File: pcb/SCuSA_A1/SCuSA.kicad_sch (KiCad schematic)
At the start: 51 parts, among them J101 USB4135-GF-A, J102 JST_S2B-PH-K-x, J103 Binding_Post_PK4_Red, J104 Binding_Post_PK4_Black, J105 Binding_Post_PK4_Red, J106 Binding_Post_PK4_Black, Q101 DMN2041LSD, SW101 JS202011CQN, SW102 JS202011CQN, U101 MCP73832T-2ACI/OT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

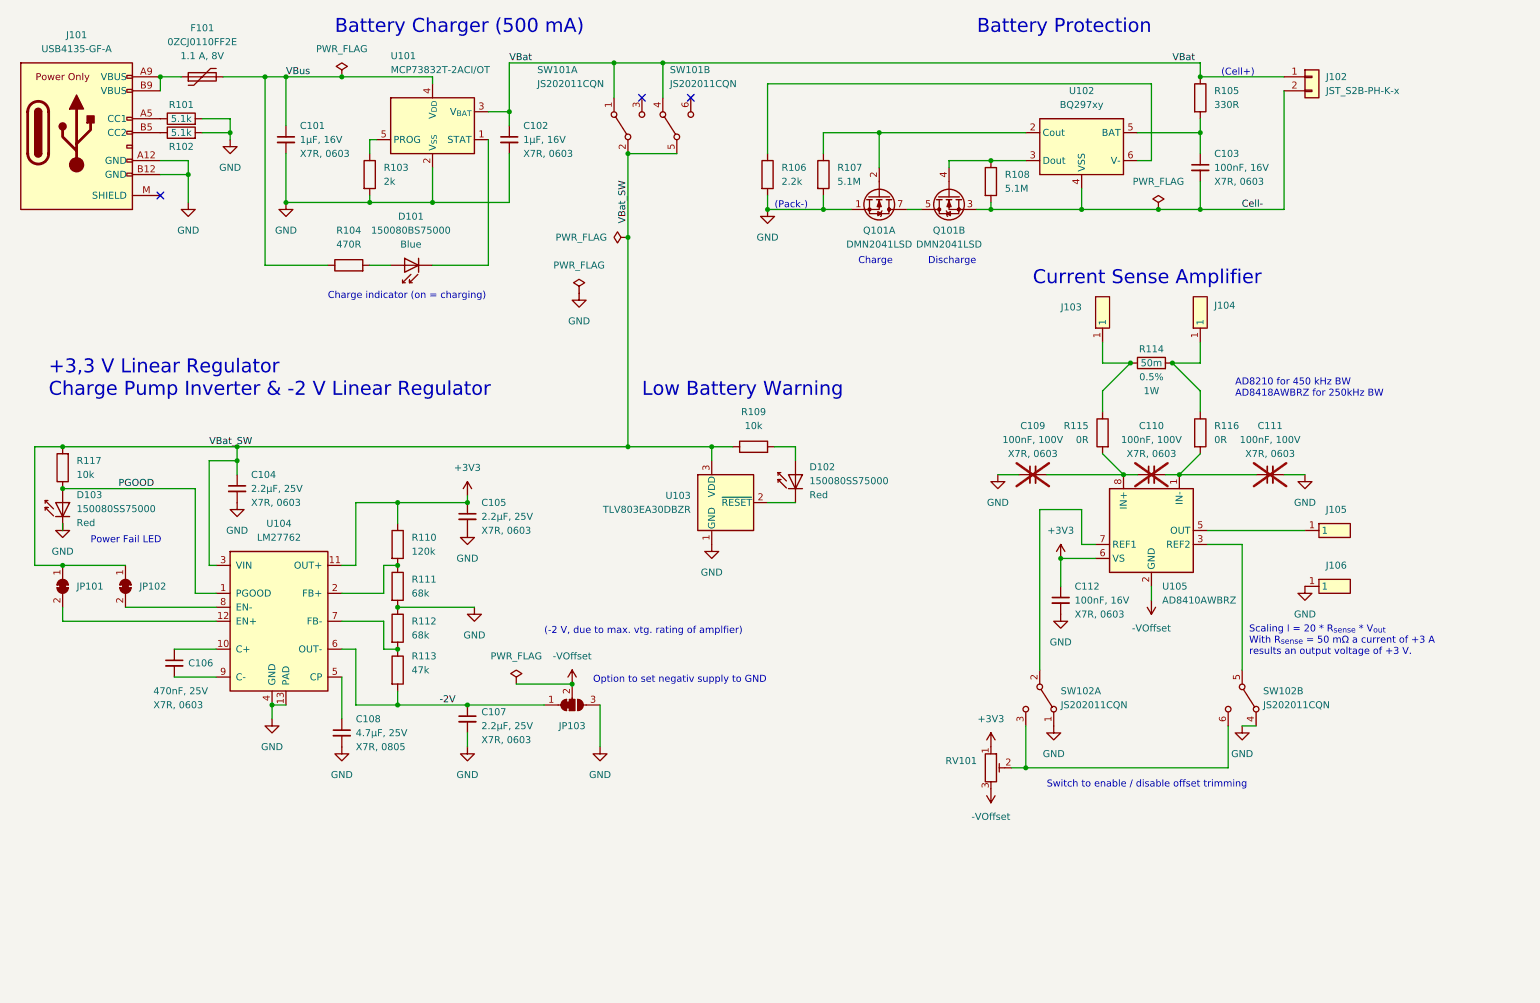
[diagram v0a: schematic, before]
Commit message: Add connectors, supply voltage filter
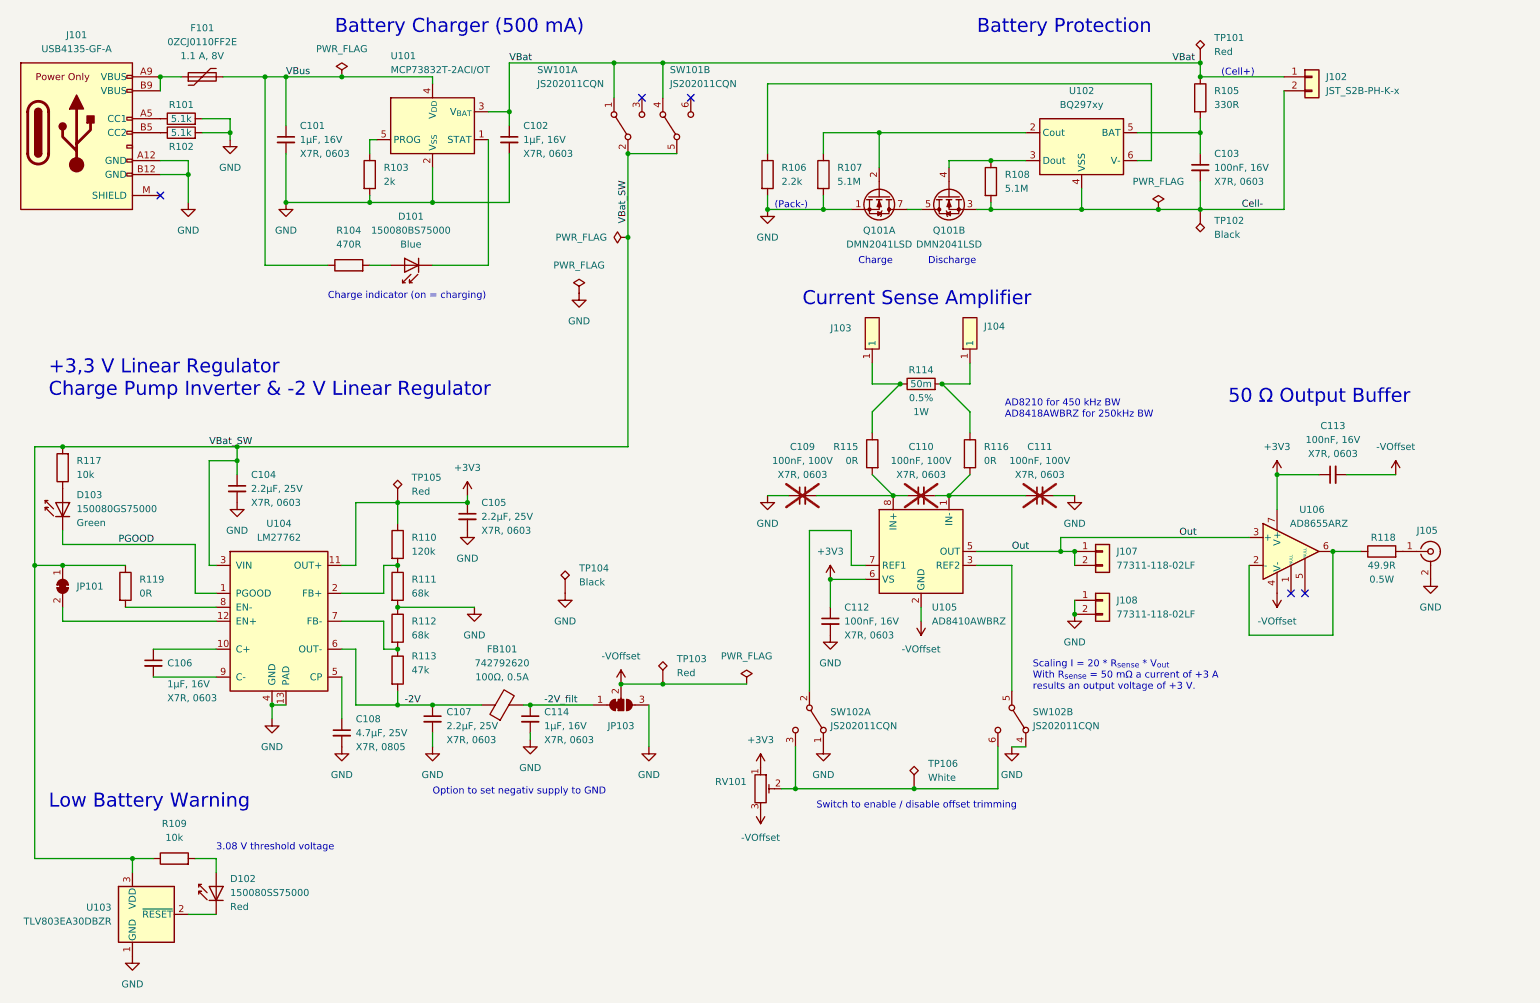
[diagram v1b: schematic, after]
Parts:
- removed D103: 150080SS75000, LED_SMD:LED_0805_2012Metric_Pad1.15x1.40mm_HandSolder, symbol LED_User:150080SS75000
- removed J105: Binding_Post_PK4_Red, Connector_User:Binding_Post_4.3mm_M4_DIN965_Pad, symbol Connector_User:Binding_Post_PK4_Red
- removed J106: Binding_Post_PK4_Black, Connector_User:Binding_Post_4.3mm_M4_DIN965_Pad, symbol Connector_User:Binding_Post_PK4_Black
- removed JP102: SolderJumper_2_Bridged, Jumper:SolderJumper-2_P1.3mm_Bridged_Pad1.0x1.5mm, symbol Jumper:SolderJumper_2_Bridged
- added C113: 100nF,16V,X7R,0603, Capacitor_SMD:C_0603_1608Metric_Pad1.08x0.95mm_HandSolder, symbol Capacitor_User:100nF,16V,X7R,0603
- added C114: 1uF,16V,X7R,0603, Capacitor_SMD:C_0603_1608Metric_Pad1.08x0.95mm_HandSolder, symbol Capacitor_User:1uF,16V,X7R,0603
- added D103: 150080GS75000, LED_SMD:LED_0805_2012Metric_Pad1.15x1.40mm_HandSolder, symbol LED_User:150080GS75000
- added FB101: 742792620, Inductor_SMD:L_1206_3216Metric_Pad1.42x1.75mm_HandSolder, symbol Ferrite_User:742792620
- added J105: SMA_Straight_Jack_Female, Connector_Coaxial:SMA_Wurth_60312002114503_Vertical, symbol Connector_User:SMA_Straight_Jack_Female
- added J107, J108: 77311-118-02LF, Connector_PinHeader_2.54mm:PinHeader_1x02_P2.54mm_Vertical, symbol Connector_User:77311-118-02LF
- added R118: 49.9R,1206, Resistor_SMD:R_1206_3216Metric_Pad1.30x1.75mm_HandSolder, symbol Resistor_User:49.9R,1206
- added R119: 0R,0603, Resistor_SMD:R_0603_1608Metric_Pad0.98x0.95mm_HandSolder, symbol Resistor_User:0R,0603
- added TP101, TP103, TP105: TestPoint_5010_Red, TestPoint:TestPoint_Loop_D2.60mm_Drill1.6mm_Beaded, symbol Testpoint_User:TestPoint_5010_Red
- added TP102, TP104: TestPoint_5011_Black, TestPoint:TestPoint_Loop_D2.60mm_Drill1.6mm_Beaded, symbol Testpoint_User:TestPoint_5011_Black
- added TP106: TestPoint_5012_White, TestPoint:TestPoint_Loop_D2.60mm_Drill1.6mm_Beaded, symbol Testpoint_User:TestPoint_5012_White
- added U106: AD8655ARZ, Package_SO:SOIC-8_3.9x4.9mm_P1.27mm, symbol Amplifier_Operational:AD8655
- C106: symbol Capacitor_User:470nF,25V,X7R,0603 -> Capacitor_User:1uF,16V,X7R,0603; Pretty Value 1 470nF, 25V -> 1μF, 16V
- R114: footprint Resistor_SMD:R_1206_3216Metric -> Resistor_SMD:R_1206_3216Metric_Pad1.30x1.75mm_HandSolder
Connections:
- net +3V3: now also C113.1, TP105.1, U106.7 (V+)
- net -2V: now also FB101.1; no longer JP103.1 (A)
- net -VOffset: now also C113.2, TP103.1, U106.4 (V-)
- net Cell-: now also TP102.1
- net GND: now also C114.2, J105.2 (Ext), J108.1 (Pin_1), J108.2 (Pin_2), TP104.1
- net PGOOD: now also D103.1 (K); no longer R117.1
- net VBat: now also TP101.1
- net VBat_SW: now also R119.1
- net Out: now reaches U105.5 (OUT)
- net Out: now also J107.1 (Pin_1), J107.2 (Pin_2), U106.3 (+)
- net at RV101.2, SW102.3 (C), SW102.6 (C): now also TP106.1
- net at U104.8 (EN-): now also R119.2
- new net: D103.2 (A), R117.1
- new net: R118.1, U106.2 (-), U106.6
- new net: J105.1 (In), R118.2
- new net -2V_filt: C114.1, FB101.2, JP103.1 (A)
- no-connect marks 3 -> 5
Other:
- note added: "3.08 V threshold voltage"
- note added: "50 Ω Output Buffer"
- note removed: "(-2 V, due to max. vtg. rating of amplfier)"
- note removed: "Power Fail LED"
- moved on the sheet: C106, C107, C109, C110, C111, C112, J103, J104, JP103, R114, R115, R116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

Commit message: Preliminary BOM
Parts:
- C106: value 470nF,25V,X7R,0603 -> 1uF,16V,X7R,0603
- R113: value 120k,0603 -> 47k,0603
- U102: value BQ297xy -> BQ29700DSER
- U104: SPN (none) -> 296-47331-1-ND; Supplier (none) -> Digi-Key
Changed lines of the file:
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@@
       (effects (font (size 1.27 1.27)))
     )
-    (property "Value" "BQ297xy" (at 214.63 33.02 0)
+    (property "Value" "BQ29700DSER" (at 214.63 33.02 0)
       (effects (font (size 1.27 1.27)))
     )
@@
     )
     (property "Datasheet" "http://www.ti.com/lit/ds/symlink/lm27762.pdf" (at 130.81 132.08 0)
+      (effects (font (size 1.27 1.27)) hide)
+    )
+    (property "Supplier" "Digi-Key" (at 67.31 121.92 0)
+      (effects (font (size 1.27 1.27)) hide)
+    )
+    (property "SPN" "296-47331-1-ND" (at 67.31 121.92 0)
       (effects (font (size 1.27 1.27)) hide)
     )
@@
       (effects (font (size 1.27 1.27)) (justify left))
     )
-    (property "Value" "120k,0603" (at 92.075 133.35 0)
+    (property "Value" "47k,0603" (at 92.075 133.35 0)
       (effects (font (size 1.27 1.27)) (justify left) hide)
     )
@@
       (effects (font (size 1.27 1.27)) (justify left))
     )
-    (property "Value" "470nF,25V,X7R,0603" (at 48.26 139.7 0)
-      (effects (font (size 1.27 1.27)) (justify left) hide)
-    )
+    (property "Value" "1uF,16V,X7R,0603" (at 48.26 139.7 0)
+      (effects (font (size 1.27 1.27)) (justify left) hide)
+    )

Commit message: Work on PCB layout
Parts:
- added TP107: TestPoint_5011_Black, TestPoint:TestPoint_Loop_D2.60mm_Drill1.6mm_Beaded, symbol Testpoint_User:TestPoint_5011_Black
- added TP108: TestPoint_5010_Red, TestPoint:TestPoint_Loop_D2.60mm_Drill1.6mm_Beaded, symbol Testpoint_User:TestPoint_5010_Red
- J103: footprint Connector_User:Binding_Post_4.3mm_M4_DIN965_Pad -> Connector_User:Binding_Post_PK4_Red
- J104: footprint Connector_User:Binding_Post_4.3mm_M4_DIN965_Pad -> Connector_User:Binding_Post_PK4_Black
- J105: footprint Connector_Coaxial:SMA_Wurth_60312002114503_Vertical -> Connector_User:SMA_Vertical
- RV101: footprint Potentionmeter_THT_User:Potentiometer_Suntan_3296W_Vertical -> Potentionmeter_THT_User:Potentiometer_Suntan_3296W_Vertical_90deg
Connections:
- net -VOffset: now also C112.2
- net GND: now also TP107.1; no longer C112.2
- net Out: now also TP108.1
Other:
- moved on the sheet: SW102A

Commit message: Edit PCB layout
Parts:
- removed JP101: SolderJumper_2_Bridged, Jumper:SolderJumper-2_P1.3mm_Bridged_Pad1.0x1.5mm, symbol Jumper:SolderJumper_2_Bridged
- added H101, H102, H103, H104: MountingHole, MountingHole:MountingHole_3.2mm_M3_DIN965, symbol Mechanical:MountingHole
- added JP101: SolderJumper_2_Open, Jumper:SolderJumper-2_P1.3mm_Open_TrianglePad1.0x1.5mm, symbol Jumper:SolderJumper_2_Open
- added R120: 0R,0603, Resistor_SMD:R_0603_1608Metric_Pad0.98x0.95mm_HandSolder, symbol Resistor_User:0R,0603
- R103: value 2k,0603 -> 10k,0603; symbol Resistor_User:2k,0603 -> Resistor_User:10k,0603; Resistance 2k -> 10k
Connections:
- net Cell-: now also JP101.2 (B)
- net GND: now also JP101.1 (A)
- net VBat_SW: now also R120.1
- net at U104.12 (EN+): now also R120.2
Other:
- note added: "Charging current ~ 100 mA"
- note added: "For battery pack with integrated protection."

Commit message: Edit PCB layout
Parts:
- JP103: value SolderJumper_3_Bridged12 -> SolderJumper_3_Open; footprint Jumper:SolderJumper-3_P1.3mm_Bridged12_Pad1.0x1.5mm_NumberLabels -> Jumper:SolderJumper-3_P2.0mm_Open_TrianglePad1.0x1.5mm_NumberLabels; symbol Jumper:SolderJumper_3_Bridged12 -> Jumper:SolderJumper_3_Open
- U104: footprint Package_SON:WSON-12-1EP_3x2mm_P0.5mm_EP1x2.65_ThermalVias -> Package_SON_User:WSON-12-1EP_3x2mm_P0.5mm_EP1x2.65_ThermalVias; symbol Regulator_SwitchedCapacitor:LM27762 -> Regulator_Switching_User:LM27762; MPN (none) -> LM27762DSSx; Manufacturer (none) -> Texas Instruments
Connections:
- net GND: no longer C109.1, C111.2
- net SNS-2: now reaches C110.2, C111.1, R116.2, U105.1 (IN-)
- net SNS+2: now reaches C109.2, C110.1, R115.2, U105.8 (IN+)
- net SNS-1: now reaches J104.1, R114.2, R116.1
- net SNS+1: now reaches J103.1, R114.1, R115.1
- net -VOffset renamed -Vx
- net -Vx: now also C109.1, C111.2
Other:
- moved on the sheet: J103, J104

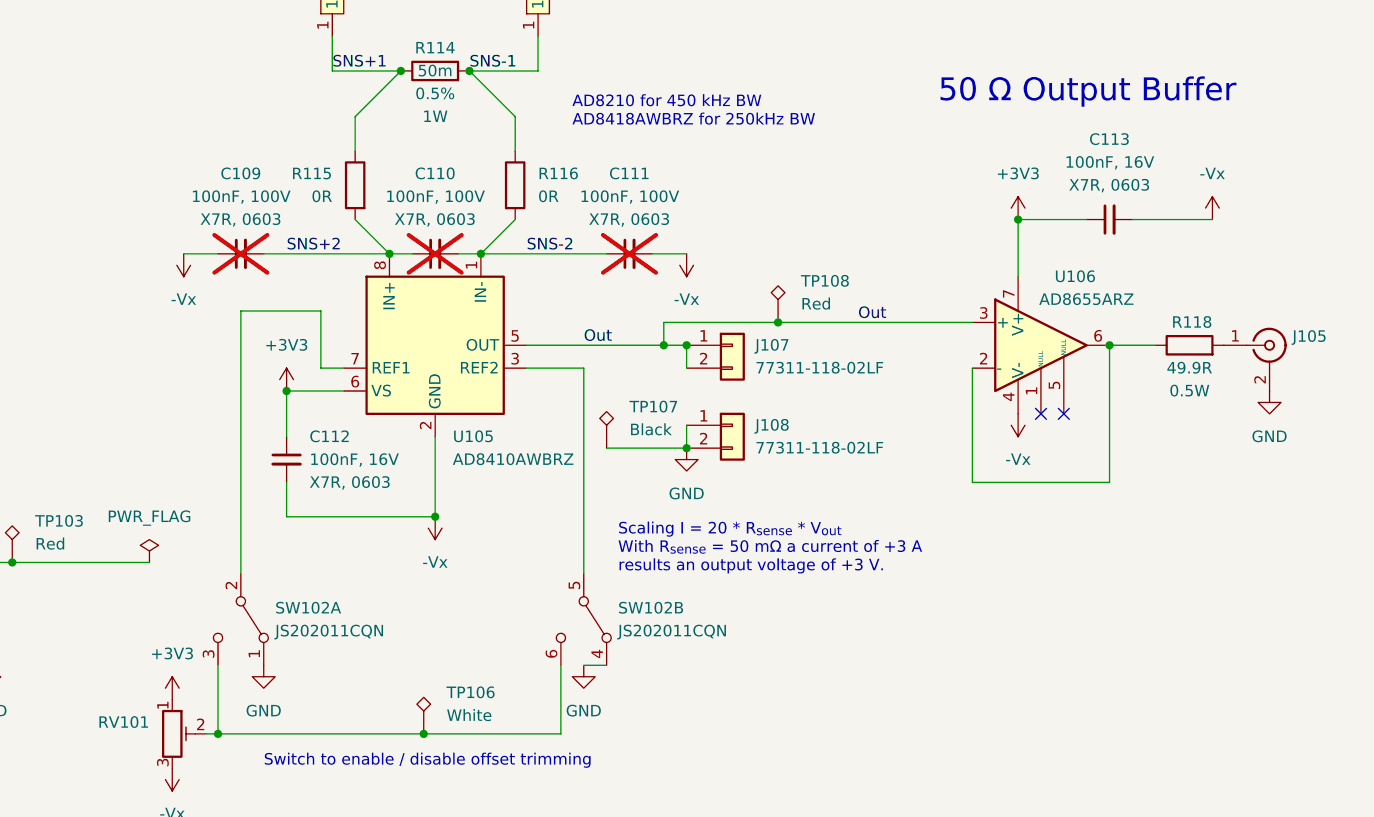
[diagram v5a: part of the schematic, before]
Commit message: Change binding posts and GND planes
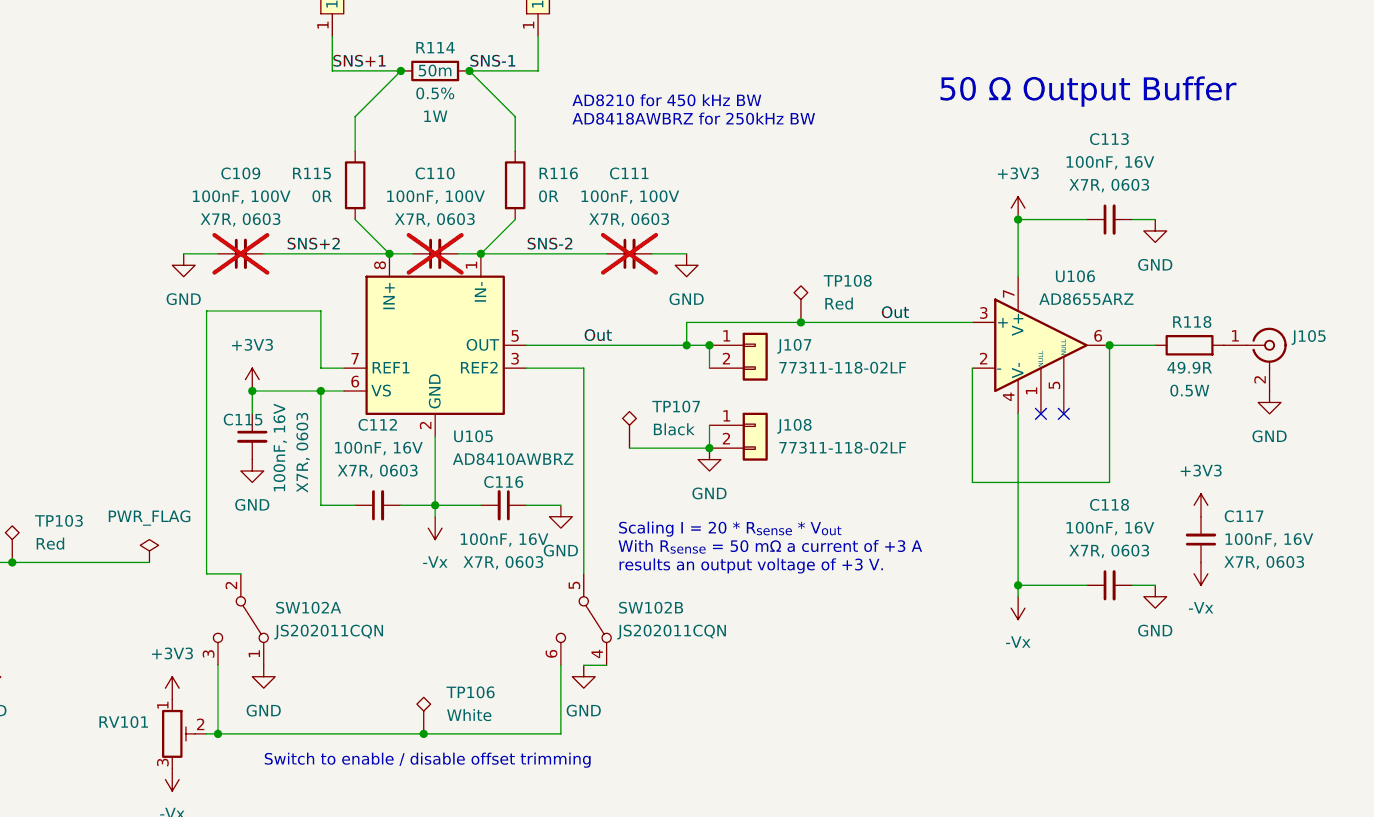
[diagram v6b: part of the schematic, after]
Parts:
- added C115, C116, C117, C118: 100nF,16V,X7R,0603, Capacitor_SMD:C_0603_1608Metric_Pad1.08x0.95mm_HandSolder, symbol Capacitor_User:100nF,16V,X7R,0603
- J103: value Binding_Post_PK4_Red -> Binding_Post_PKI_10_A_Au; footprint Connector_User:Binding_Post_PK4_Red -> Connector_User:Binding_Post_PKI_10_A_Au_Red; symbol Connector_User:Binding_Post_PK4_Red -> Connector_User:Binding_Post_PKI_10_A_Au_Red; MPN (none) -> 930103701; Manufacturer (none) -> SKS, Hirschmann; SPN PK 4 RT -> PKI 10 A AU RT
- J104: value Binding_Post_PK4_Black -> Binding_Post_PKI_10_A_Au; footprint Connector_User:Binding_Post_PK4_Black -> Connector_User:Binding_Post_PKI_10_A_Au_Black; symbol Connector_User:Binding_Post_PK4_Black -> Connector_User:Binding_Post_PKI_10_A_Au_Black; MPN (none) -> 930103700; Manufacturer (none) -> SKS, Hirschmann; SPN PK 4 SW -> PKI 10 A AU SW
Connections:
- net +3V3: now also C115.1, C117.2
- net -Vx: now also C116.2, C117.1, C118.1; no longer C109.1, C111.2, C113.2
- net GND: now also C109.1, C111.2, C113.2, C115.2, C116.1, C118.2
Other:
- moved on the sheet: C112, J107, J108, TP107, TP108

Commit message: Edit PCB layout
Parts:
- removed TP103, TP105: TestPoint_5010_Red, TestPoint:TestPoint_Loop_D2.60mm_Drill1.6mm_Beaded, symbol Testpoint_User:TestPoint_5010_Red
- added C119: 1uF,16V,X7R,0603, Capacitor_SMD:C_0603_1608Metric_Pad1.08x0.95mm_HandSolder, symbol Capacitor_User:1uF,16V,X7R,0603
- added FB100: 742792620, Inductor_SMD:L_1206_3216Metric_Pad1.42x1.75mm_HandSolder, symbol Ferrite_User:742792620
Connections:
- net +3V3: now also C119.1, FB100.2; no longer C105.1, R110.1, U104.11 (OUT+)
- net GND: now also C119.2
- new net: C105.1, FB100.1, R110.1, U104.11 (OUT+)
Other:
- moved on the sheet: C105, TP104
